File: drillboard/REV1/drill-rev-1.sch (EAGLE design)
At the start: 41 parts, among them M1 M03VERT, M2 M03VERT, M3 M03VERT, M4 M03VERT, T1 M03VERT, T2 M03VERT, T3 M03VERT, T4 M03VERT

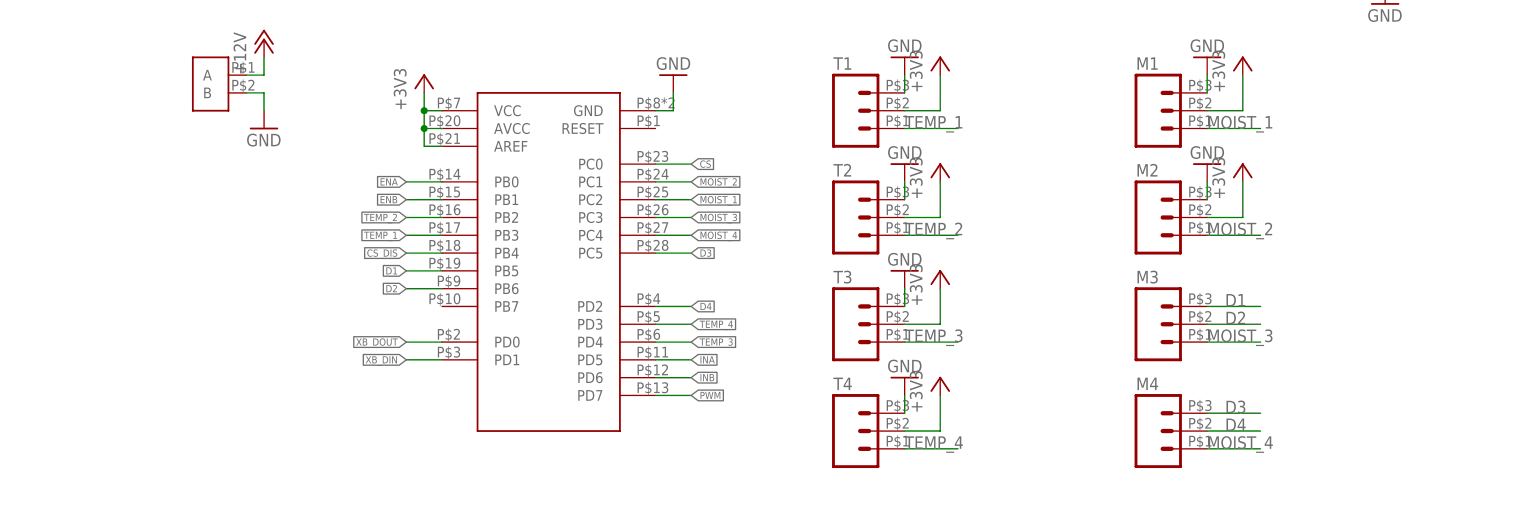
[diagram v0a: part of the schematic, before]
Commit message: made modifications for testing
- moved pwm to PD6
- moved INB to PB5
- removed custom moisture sensor M3
- added crystal oscillator to ATMEGA328p
- added resistors to make moisture sensor M4 work
NOTE: These changes were added post-production and were not actually
incorporated in the REV3 board. Disregard board design, schematic
changed for reference only.
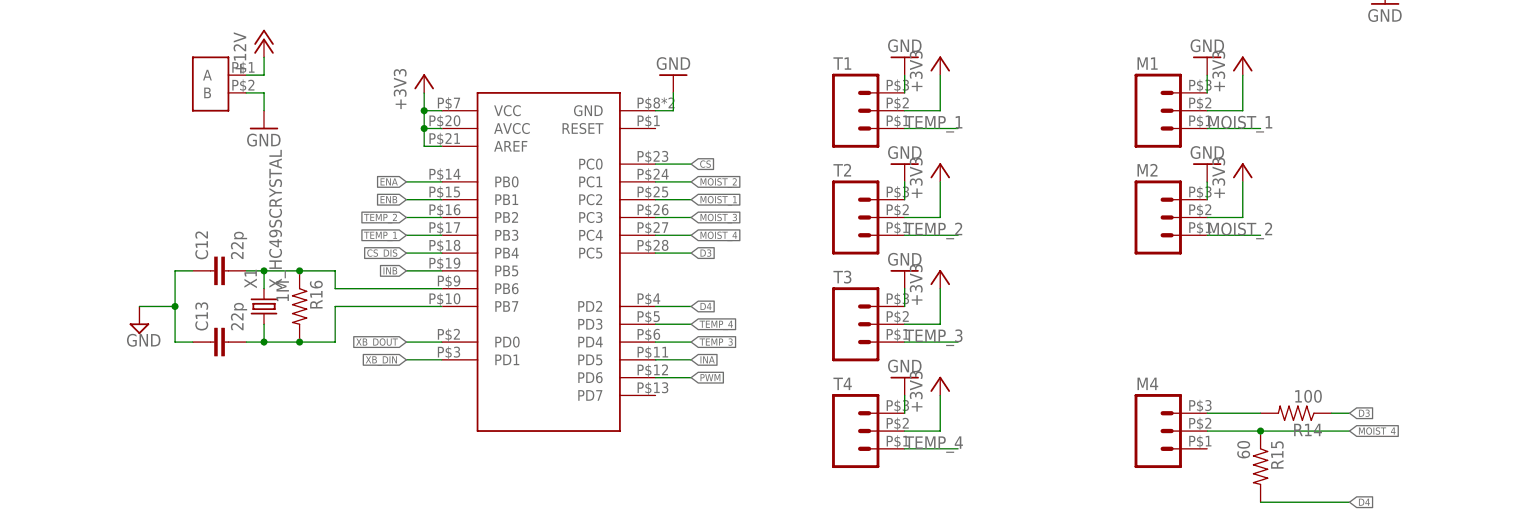
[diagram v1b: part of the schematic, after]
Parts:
- removed M3: M03VERT, MRDT-Connectors:M03VERT
- added C12, C13: 22p, SparkFun-Passives:CAP0603-CAP
- added R14: 100, SparkFun-Resistors:RESISTOR1206
- added R15: 60, SparkFun-Resistors:RESISTOR1206
- added R16: 1M, SparkFun-Resistors:RESISTOR0603
- added X1: X_HC49SCRYSTAL, MRDT-2014-All:X_HC49SCRYSTAL
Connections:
- removed net D1: M3.3, U$13.PB5
- removed net D2: M3.2, U$13.PB6
- new net N$1: M4.3, R14.2
- new net XTAL1: C12.2, R16.1, U$13.PB6, X1.2
- new net XTAL2: C13.2, R16.2, U$13.PB7, X1.1
- net D3: now also R14.1; no longer M4.3
- net D4: now also R15.2; no longer M4.2
- net GND: now also C12.1, C13.1
- net INB: now also U$13.PB5; no longer U$13.PD6
- net MOIST_3: no longer M3.1
- net MOIST_4: now also M4.2, R15.1; no longer M4.1
- net PWM: now also U$13.PD6; no longer U$13.PD7

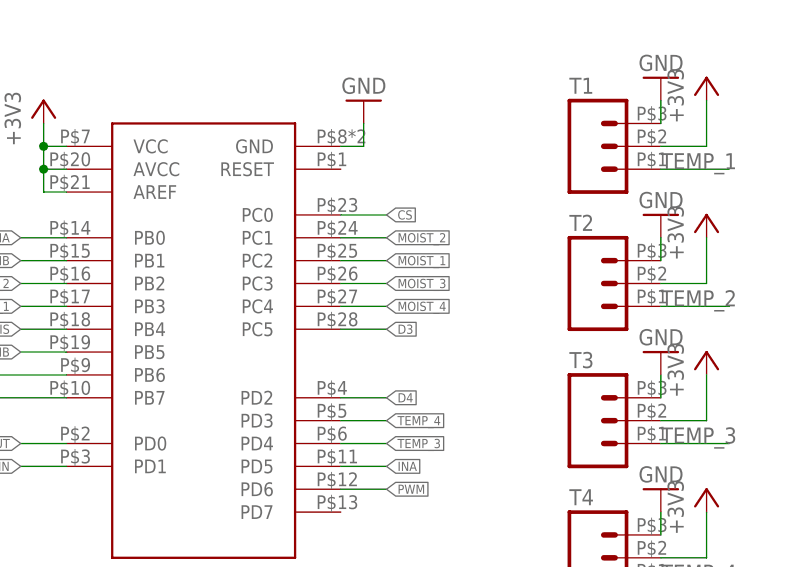
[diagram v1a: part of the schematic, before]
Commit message: removed MOIST_3 net from sch
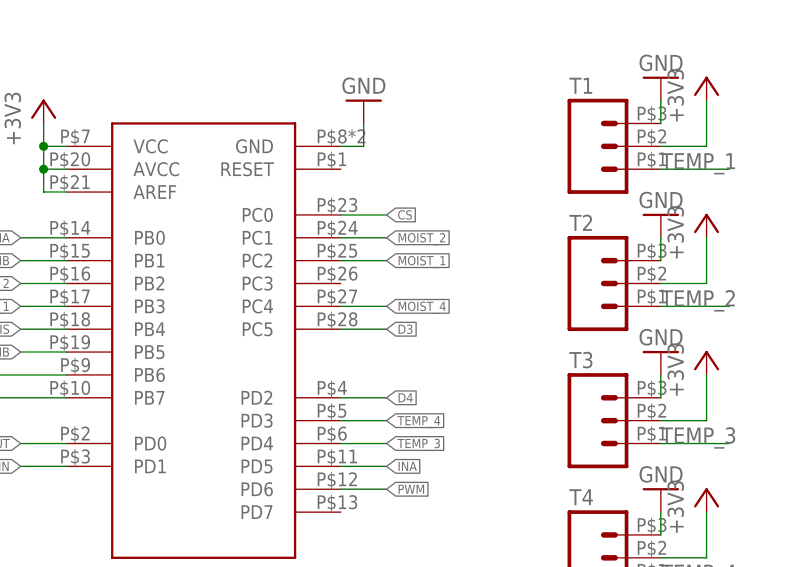
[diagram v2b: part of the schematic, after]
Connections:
- removed net MOIST_3: U$13.PC3
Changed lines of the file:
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@@
-</segment>
-</net>
-<net name="MOIST_3" class="0">
-<segment>
-<pinref part="U$13" gate="G$1" pin="PC3"/>
-<wire x1="137.16" y1="-40.64" x2="142.24" y2="-40.64" width="0.1524" layer="91"/>
-<label x="142.24" y="-40.64" size="1.016" layer="95" xref="yes"/>
 </segment>
 </net>
